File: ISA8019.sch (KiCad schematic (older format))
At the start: 53 parts, among them J1 Bus_ISA_8bit, J2 8P8C_Shielded, J4 Jumper mode, J5 PNP force, J6 BROM size and base address, J7 I/O base address, J8 Medium type, J9 IRQ Select, T1 13F-39MNL, U1 RTL8019AS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

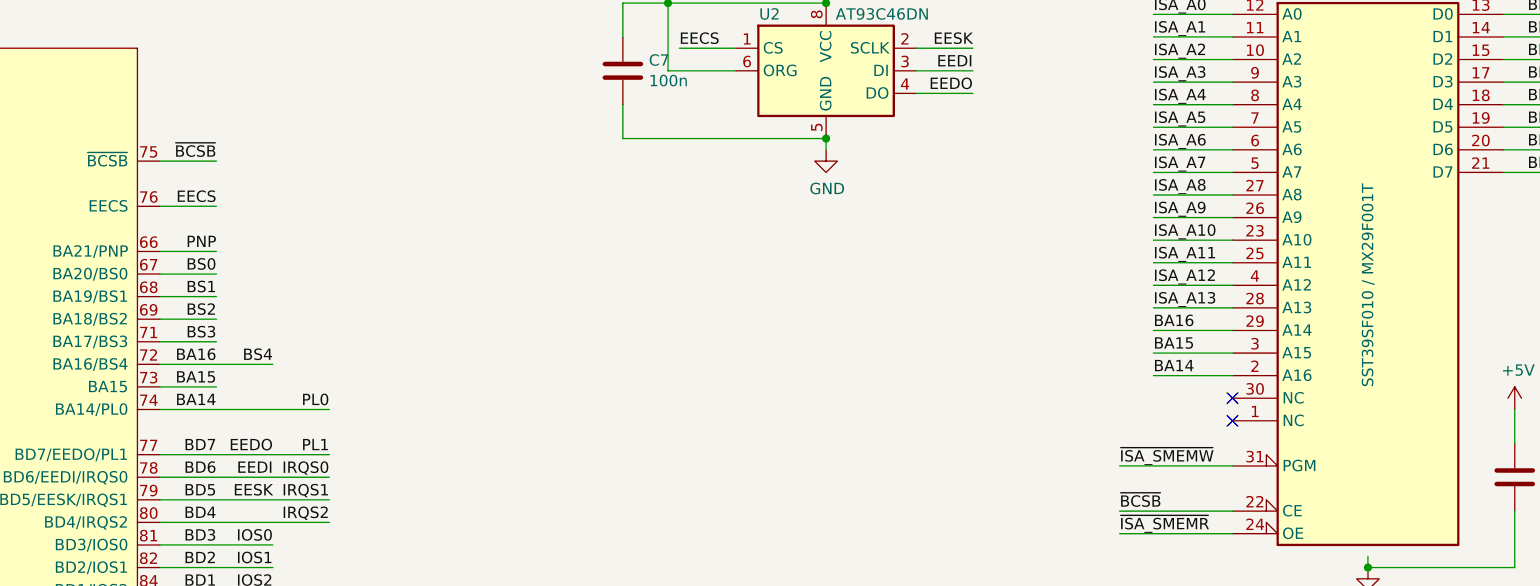
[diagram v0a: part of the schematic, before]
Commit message: Add rev 2.2, supporting an 30SF040 EPROM, also additional address lines are now broken out
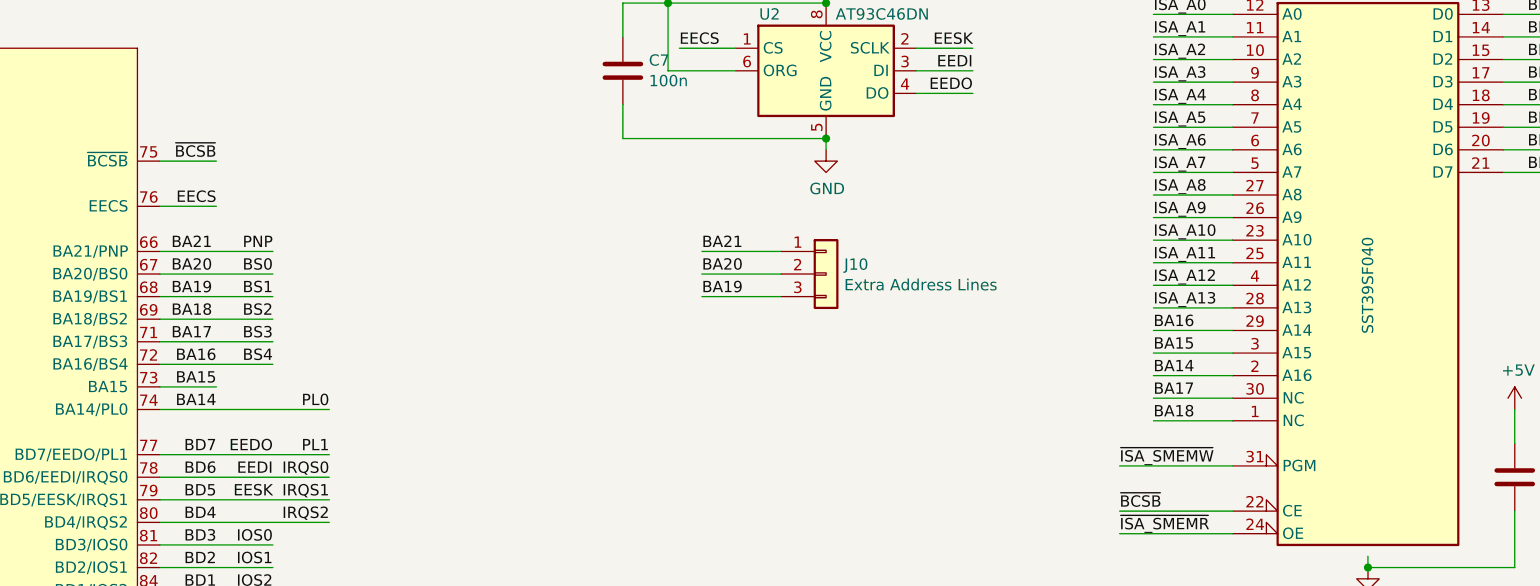
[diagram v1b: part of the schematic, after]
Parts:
- added J10: Extra Address Lines, Connector_PinHeader_2.54mm:PinHeader_1x03_P2.54mm_Vertical, symbol Connector_Generic:Conn_01x03
- U3: value SST39SF010 / MX29F001T -> SST39SF040
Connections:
- net BS2 is gone; now on net BA18: R11.1, U1.69 (BA18/BS2)
- net BS3 is gone; now on net BA17: R12.1, U1.71 (BA17/BS3)
- net BA18: now reaches U3.1 (NC)
- net BA17: now reaches U3.30 (NC)
- net BS0 renamed BA20
- net BA20: now also J10.2 (Pin_2)
- net BS1 renamed BA19
- net BA19: now also J10.3 (Pin_3)
- net PNP renamed BA21
- net BA21: now also J10.1 (Pin_1)
- no-connect marks 6 -> 4
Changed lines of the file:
@@
 Title "ISA8019"
 Date "2020-11-12"
-Rev "A"
+Rev "2.2"
 Comp "tbspace.de"
 Comment1 "Tobias Mädel"
@@
 Wire Wire Line
 	14050 1750 14200 1750
-Text Label 7600 2400 2    50   ~ 0
+Text Label 7850 2400 2    50   ~ 0
 PNP
-Wire Wire Line
-	7350 2400 7600 2400
 Text Label 13950 2100 0    50   ~ 0
 PNP
 Wire Wire Line
 	14200 2100 13950 2100
-Text Label 7600 2500 2    50   ~ 0
+Text Label 7850 2500 2    50   ~ 0
 BS0
-Text Label 7600 2600 2    50   ~ 0
+Text Label 7850 2600 2    50   ~ 0
 BS1
-Text Label 7600 2700 2    50   ~ 0
-BS2
-Text Label 7600 2800 2    50   ~ 0
-BS3
 Text Label 7850 2900 2    50   ~ 0
 BS4
-Wire Wire Line
-	7600 2800 7350 2800
-Wire Wire Line
-	7350 2700 7600 2700
-Wire Wire Line
-	7600 2600 7350 2600
-Wire Wire Line
-	7350 2500 7600 2500
 Text Label 13950 2450 0    50   ~ 0
 BS0
@@
 Text Label 13550 2050 2    50   ~ 0
 BD7
-NoConn ~ 12100 3150
-NoConn ~ 12100 3050
 Wire Wire Line
 	11600 3550 12100 3550
@@
 P 12700 2550
 F 0 "U3" H 12350 3850 50  0000 C CNN
-F 1 "SST39SF010 / MX29F001T" V 12700 2550 50  0000 C CNN
+F 1 "SST39SF040" V 12700 2550 50  0000 C CNN
 F 2 "Package_DIP:DIP-32_W15.24mm_Socket" H 12700 2850 50  0001 C CNN
 F 3 "http://ww1.microchip.com/downloads/en/DeviceDoc/25022B.pdf" H 12700 2850 50  0001 C CNN
@@
 	15550 4500 15550 4400
 Connection ~ 15550 4400
+Wire Wire Line
+	11750 3150 12100 3150
+Wire Wire Line
+	11750 3050 12100 3050
+Text Label 11750 3050 0    50   ~ 0
+BA17
+Text Label 11750 3150 0    50   ~ 0
+BA18
+Text Label 7850 2800 2    50   ~ 0
+BS3
+Text Label 7850 2700 2    50   ~ 0
+BS2
+Wire Wire Line
+	7350 2400 7850 2400
+Wire Wire Line
+	7350 2500 7850 2500
+Wire Wire Line
+	7350 2600 7850 2600
+Wire Wire Line
+	7350 2700 7850 2700
+Wire Wire Line
+	7350 2800 7850 2800
+Text Label 7400 2800 0    50   ~ 0
+BA17
+Text Label 7400 2700 0    50   ~ 0
+BA18
+Text Label 7400 2600 0    50   ~ 0
+BA19
+Text Label 7400 2500 0    50   ~ 0
+BA20
+Text Label 7400 2400 0    50   ~ 0
+BA21
+$Comp
+L Connector_Generic:Conn_01x03 J10
+U 1 1 60D56932
+P 10300 2500
+F 0 "J10" H 10380 2542 50  0000 L CNN
+F 1 "Extra Address Lines" H 10380 2451 50  0000 L CNN
+F 2 "Connector_PinHeader_2.54mm:PinHeader_1x03_P2.54mm_Vertical" H 10300 2500 50  0001 C CNN
+F 3 "~" H 10300 2500 50  0001 C CNN
+	1    10300 2500
+	1    0    0    -1
+$EndComp
+Wire Wire Line
+	9750 2600 10100 2600
+Text Label 9750 2600 0    50   ~ 0
+BA19
+Wire Wire Line
+	9750 2400 10100 2400
+Wire Wire Line
+	9750 2500 10100 2500
+Text Label 9750 2500 0    50   ~ 0
+BA20
+Text Label 9750 2400 0    50   ~ 0
+BA21
 $EndSCHEMATC

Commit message: Fix address BA14/16 ordering to SST39SF040
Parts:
- U3: symbol Memory_Flash:SST39SF010 -> Memory_Flash:SST39SF040
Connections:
- net BA14: now also U3.29 (A14); no longer U3.2 (A16)
- net BA16: now also U3.2 (A16); no longer U3.29 (A14)
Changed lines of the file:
@@
 ~BCSB
 Wire Wire Line
-	11750 2950 12100 2950
+	11750 2750 12100 2750
 Wire Wire Line
 	11750 2850 12100 2850
 Wire Wire Line
-	11750 2750 12100 2750
-Text Label 11750 2750 0    50   ~ 0
+	11750 2950 12100 2950
+Text Label 11750 2950 0    50   ~ 0
 BA16
 Text Label 11750 2850 0    50   ~ 0
 BA15
-Text Label 11750 2950 0    50   ~ 0
+Text Label 11750 2750 0    50   ~ 0
 BA14
 Wire Wire Line
@@
 $EndComp
 $Comp
-L Memory_Flash:SST39SF010 U3
+L Memory_Flash:SST39SF040 U3
 U 1 1 602BB235
 P 12700 2550
